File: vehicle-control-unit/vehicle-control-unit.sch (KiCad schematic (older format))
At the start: 22 parts, among them J1 Conn_02x04_Male_UnitPerRow, J2 Conn_01x04_Male, J3 Conn_02x03_Male, J4 Conn_02x03_Male, J5 Conn_02x03_Male, J6 Conn_02x03_Male, U1 Teensy3.2, U2 NRF24L01+ breakout

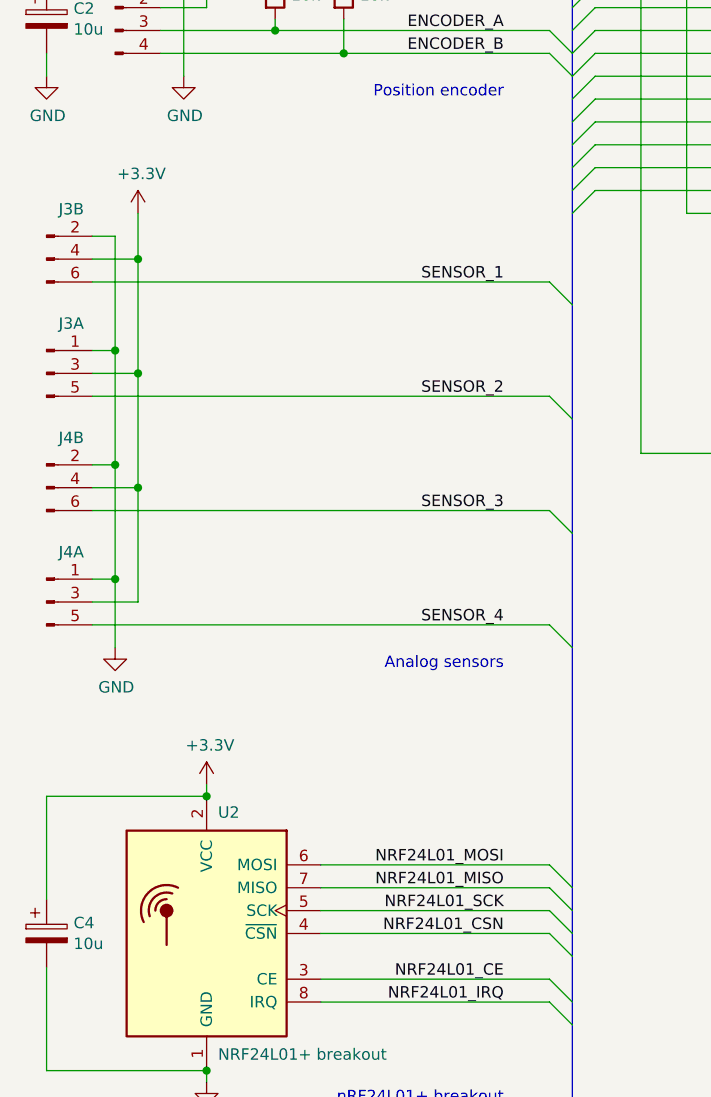
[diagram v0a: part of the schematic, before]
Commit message: Clean up routing
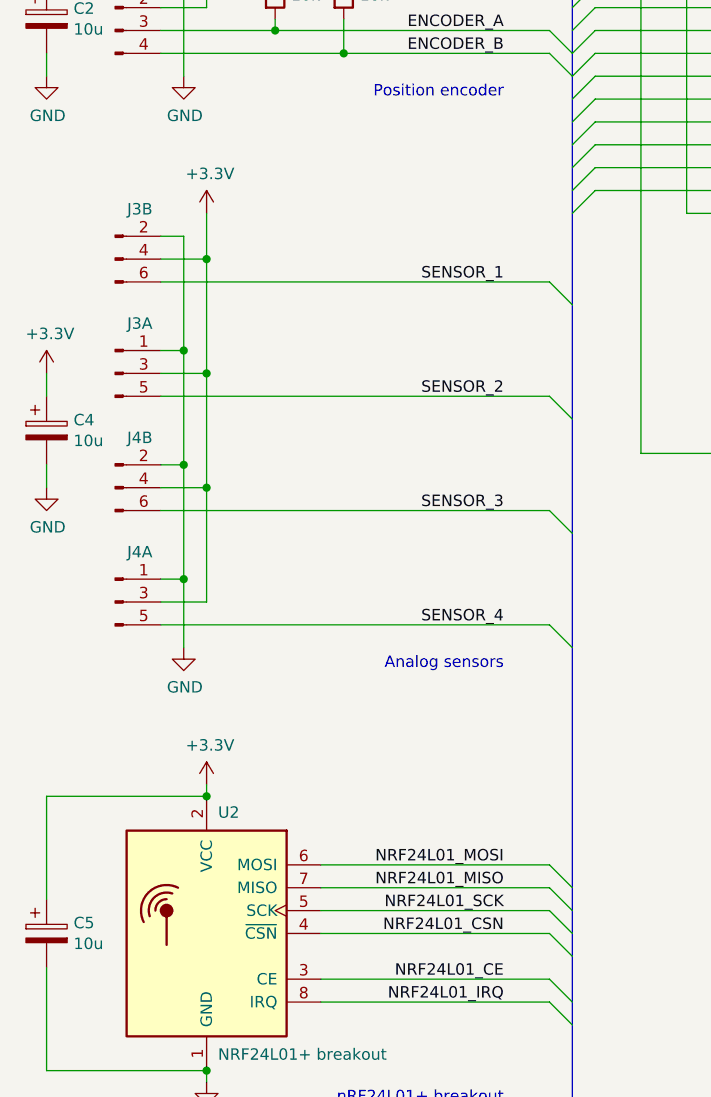
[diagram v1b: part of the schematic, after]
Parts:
- added C4: 10u, Capacitor_THT:CP_Radial_D5.0mm_P2.50mm, symbol Device:CP
- renumbered C4 to C5
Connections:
- net +3V3: now also C4.1
- net GND: now also C4.2
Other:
- moved on the sheet: J3A, J3B, J4A, J4B
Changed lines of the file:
@@
 Sheet 1 3
 Title "Earth Rover"
-Date "2020-06-07"
-Rev "7"
+Date "2020-06-08"
+Rev "8"
 Comp "Vijfendertig BVBA"
 Comment1 "Maarten De Munck"
@@
 	6850 6350 6850 6950
 $Comp
-L power:GND #PWR021
+L power:GND #PWR023
 U 1 1 5DE14910
 P 6850 8250
-F 0 "#PWR021" H 6850 8000 50  0001 C CNN
+F 0 "#PWR023" H 6850 8000 50  0001 C CNN
 F 1 "GND" H 6855 8077 50  0000 C CNN
 F 2 "" H 6850 8250 50  0001 C CNN
@@
 Connection ~ 6650 5950
 $Comp
-L power:+5V #PWR018
+L power:+5V #PWR019
 U 1 1 5DE1FF8F
 P 6650 5850
-F 0 "#PWR018" H 6650 5700 50  0001 C CNN
+F 0 "#PWR019" H 6650 5700 50  0001 C CNN
 F 1 "+5V" H 6665 6023 50  0000 C CNN
 F 2 "" H 6650 5850 50  0001 C CNN
@@
 L earth-rover-symbols:Conn_02x03_Male_UnitPerRow J3
 U 2 1 5DFC88C9
-P 1250 5000
-F 0 "J3" H 1358 5189 50  0000 C BNN
-F 1 "Conn_02x03_Male" H 1358 5190 50  0001 C CNN
-F 2 "Connector_PinHeader_2.54mm:PinHeader_2x03_P2.54mm_Horizontal" H 1250 5000 50  0001 C CNN
-F 3 "~" H 1250 5000 50  0001 C CNN
-	2    1250 5000
-	1    0    0    -1
-$EndComp
-$Comp
-L power:GND #PWR019
+P 1550 5000
+F 0 "J3" H 1658 5189 50  0000 C BNN
+F 1 "Conn_02x03_Male" H 1658 5190 50  0001 C CNN
+F 2 "Connector_PinHeader_2.54mm:PinHeader_2x03_P2.54mm_Horizontal" H 1550 5000 50  0001 C CNN
+F 3 "~" H 1550 5000 50  0001 C CNN
+	2    1550 5000
+	1    0    0    -1
+$EndComp
+$Comp
+L power:GND #PWR021
 U 1 1 5DFCC639
-P 1550 6700
-F 0 "#PWR019" H 1550 6450 50  0001 C CNN
-F 1 "GND" H 1555 6527 50  0000 C CNN
-F 2 "" H 1550 6700 50  0001 C CNN
-F 3 "" H 1550 6700 50  0001 C CNN
-	1    1550 6700
+P 1850 6700
+F 0 "#PWR021" H 1850 6450 50  0001 C CNN
+F 1 "GND" H 1855 6527 50  0000 C CNN
+F 2 "" H 1850 6700 50  0001 C CNN
+F 3 "" H 1850 6700 50  0001 C CNN
+	1    1850 6700
 	1    0    0    -1
 $EndComp
@@
 L power:+3.3V #PWR016
 U 1 1 5DFCCB63
-P 1650 4800
-F 0 "#PWR016" H 1650 4650 50  0001 C CNN
-F 1 "+3.3V" H 1665 4973 50  0000 C CNN
-F 2 "" H 1650 4800 50  0001 C CNN
-F 3 "" H 1650 4800 50  0001 C CNN
-	1    1650 4800
-	1    0    0    -1
-$EndComp
-Wire Wire Line
-	1450 4900 1550 4900
-Wire Wire Line
-	1550 4900 1550 5400
-Wire Wire Line
-	1450 5000 1650 5000
-Wire Wire Line
-	1650 5000 1650 4800
+P 1950 4800
+F 0 "#PWR016" H 1950 4650 50  0001 C CNN
+F 1 "+3.3V" H 1965 4973 50  0000 C CNN
+F 2 "" H 1950 4800 50  0001 C CNN
+F 3 "" H 1950 4800 50  0001 C CNN
+	1    1950 4800
+	1    0    0    -1
+$EndComp
+Wire Wire Line
+	1750 4900 1850 4900
+Wire Wire Line
+	1850 4900 1850 5400
+Wire Wire Line
+	1750 5000 1950 5000
+Wire Wire Line
+	1950 5000 1950 4800
 $Comp
 L earth-rover-symbols:Conn_02x03_Male_UnitPerRow J3
 U 1 1 5E000766
-P 1250 5500
-F 0 "J3" H 1358 5689 50  0000 C BNN
-F 1 "Conn_02x03_Male" H 1358 5690 50  0001 C CNN
-F 2 "Connector_PinHeader_2.54mm:PinHeader_2x03_P2.54mm_Horizontal" H 1250 5500 50  0001 C CNN
-F 3 "~" H 1250 5500 50  0001 C CNN
-	1    1250 5500
+P 1550 5500
+F 0 "J3" H 1658 5689 50  0000 C BNN
+F 1 "Conn_02x03_Male" H 1658 5690 50  0001 C CNN
+F 2 "Connector_PinHeader_2.54mm:PinHeader_2x03_P2.54mm_Horizontal" H 1550 5500 50  0001 C CNN
+F 3 "~" H 1550 5500 50  0001 C CNN
+	1    1550 5500
 	1    0    0    -1
 $EndComp
@@
 L earth-rover-symbols:Conn_02x03_Male_UnitPerRow J4
 U 2 1 5E000E2E
-P 1250 6000
-F 0 "J4" H 1358 6189 50  0000 C BNN
-F 1 "Conn_02x03_Male" H 1358 6190 50  0001 C CNN
-F 2 "Connector_PinHeader_2.54mm:PinHeader_2x03_P2.54mm_Horizontal" H 1250 6000 50  0001 C CNN
-F 3 "~" H 1250 6000 50  0001 C CNN
-	2    1250 6000
+P 1550 6000
+F 0 "J4" H 1658 6189 50  0000 C BNN
+F 1 "Conn_02x03_Male" H 1658 6190 50  0001 C CNN
+F 2 "Connector_PinHeader_2.54mm:PinHeader_2x03_P2.54mm_Horizontal" H 1550 6000 50  0001 C CNN
+F 3 "~" H 1550 6000 50  0001 C CNN
+	2    1550 6000
 	1    0    0    -1
 $EndComp
@@
 L earth-rover-symbols:Conn_02x03_Male_UnitPerRow J4
 U 1 1 5E0013EA
-P 1250 6500
-F 0 "J4" H 1358 6689 50  0000 C BNN
-F 1 "Conn_02x03_Male" H 1358 6690 50  0001 C CNN
-F 2 "Connector_PinHeader_2.54mm:PinHeader_2x03_P2.54mm_Horizontal" H 1250 6500 50  0001 C CNN
-F 3 "~" H 1250 6500 50  0001 C CNN
-	1    1250 6500
-	1    0    0    -1
-$EndComp
-Wire Wire Line
-	1450 5400 1550 5400
-Connection ~ 1550 5400
-Wire Wire Line
-	1550 5400 1550 5900
-Wire Wire Line
-	1450 5900 1550 5900
-Connection ~ 1550 5900
-Wire Wire Line
-	1550 5900 1550 6400
-Wire Wire Line
-	1450 6400 1550 6400
-Connection ~ 1550 6400
-Wire Wire Line
-	1550 6400 1550 6700
-Wire Wire Line
-	1650 5000 1650 5500
-Wire Wire Line
-	1650 5500 1450 5500
-Connection ~ 1650 5000
-Wire Wire Line
-	1650 5500 1650 6000
-Wire Wire Line
-	1650 6000 1450 6000
-Connection ~ 1650 5500
-Wire Wire Line
-	1650 6000 1650 6500
-Wire Wire Line
-	1650 6500 1450 6500
-Connection ~ 1650 6000
-$Comp
-L power:GND #PWR022
+P 1550 6500
+F 0 "J4" H 1658 6689 50  0000 C BNN
+F 1 "Conn_02x03_Male" H 1658 6690 50  0001 C CNN
+F 2 "Connector_PinHeader_2.54mm:PinHeader_2x03_P2.54mm_Horizontal" H 1550 6500 50  0001 C CNN
+F 3 "~" H 1550 6500 50  0001 C CNN
+	1    1550 6500
+	1    0    0    -1
+$EndComp
+Wire Wire Line
+	1750 5400 1850 5400
+Connection ~ 1850 5400
+Wire Wire Line
+	1850 5400 1850 5900
+Wire Wire Line
+	1750 5900 1850 5900
+Connection ~ 1850 5900
+Wire Wire Line
+	1850 5900 1850 6400
+Wire Wire Line
+	1750 6400 1850 6400
+Connection ~ 1850 6400
+Wire Wire Line
+	1850 6400 1850 6700
+Wire Wire Line
+	1950 5000 1950 5500
+Wire Wire Line
+	1950 5500 1750 5500
+Connection ~ 1950 5000
+Wire Wire Line
+	1950 5500 1950 6000
+Wire Wire Line
+	1950 6000 1750 6000
+Connection ~ 1950 5500
+Wire Wire Line
+	1950 6000 1950 6500
+Wire Wire Line
+	1950 6500 1750 6500
+Connection ~ 1950 6000
+$Comp
+L power:GND #PWR024
 U 1 1 5DFBDB8E
 P 1950 8600
-F 0 "#PWR022" H 1950 8350 50  0001 C CNN
+F 0 "#PWR024" H 1950 8350 50  0001 C CNN
 F 1 "GND" H 1955 8427 50  0000 C CNN
 F 2 "" H 1950 8600 50  0001 C CNN
@@
 $EndComp
 $Comp
-L power:+3.3V #PWR020
+L power:+3.3V #PWR022
 U 1 1 5DFBD20A
 P 1950 7300
-F 0 "#PWR020" H 1950 7150 50  0001 C CNN
+F 0 "#PWR022" H 1950 7150 50  0001 C CNN
 F 1 "+3.3V" H 1965 7473 50  0000 C CNN
 F 2 "" H 1950 7300 50  0001 C CNN
@@
 $EndComp
 $Comp
-L power:GND #PWR024
+L power:GND #PWR026
 U 1 1 5E17642F
 P 1350 9700
-F 0 "#PWR024" H 1350 9450 50  0001 C CNN
+F 0 "#PWR026" H 1350 9450 50  0001 C CNN
 F 1 "GND" H 1355 9527 50  0000 C CNN
 F 2 "" H 1350 9700 50  0001 C CNN
@@
 $EndComp
 $Comp
-L power:+3.3V #PWR023
+L power:+3.3V #PWR025
 U 1 1 5E177C83
 P 1950 9200
-F 0 "#PWR023" H 1950 9050 50  0001 C CNN
+F 0 "#PWR025" H 1950 9050 50  0001 C CNN
 F 1 "+3.3V" H 1965 9373 50  0000 C CNN
 F 2 "" H 1950 9200 50  0001 C CNN
@@
 $EndComp
 $Comp
-L Device:CP C4
+L Device:CP C5
 U 1 1 5DE41454
 P 1250 7950
-F 0 "C4" H 1368 7996 50  0000 L CNN
+F 0 "C5" H 1368 7996 50  0000 L CNN
 F 1 "10u" H 1368 7905 50  0000 L CNN
 F 2 "Capacitor_THT:CP_Radial_D5.0mm_P2.50mm" H 1288 7800 50  0001 C CNN
@@
 	1950 9600 3450 9600
 Wire Wire Line
-	1450 6600 3450 6600
-Wire Wire Line
-	1450 6100 3450 6100
-Wire Wire Line
-	1450 5600 3450 5600
-Wire Wire Line
-	1450 5100 3450 5100
+	1750 6600 3450 6600
+Wire Wire Line
+	1750 6100 3450 6100
+Wire Wire Line
+	1750 5600 3450 5600
+Wire Wire Line
+	1750 5100 3450 5100
 Wire Wire Line
 	2550 2800 3450 2800
@@
 Text Notes 3250 4300 2    50   ~ 0
 Position encoder
+$Comp
+L Device:CP C4
+U 1 1 5EE06376
+P 1250 5750
+F 0 "C4" H 1368 5796 50  0000 L CNN
+F 1 "10u" H 1368 5705 50  0000 L CNN
+F 2 "Capacitor_THT:CP_Radial_D5.0mm_P2.50mm" H 1288 5600 50  0001 C CNN
+F 3 "~" H 1250 5750 50  0001 C CNN
+	1    1250 5750
+	1    0    0    -1
+$EndComp
+$Comp
+L power:GND #PWR020
+U 1 1 5EE0637C
+P 1250 6000
+F 0 "#PWR020" H 1250 5750 50  0001 C CNN
+F 1 "GND" H 1255 5827 50  0000 C CNN
+F 2 "" H 1250 6000 50  0001 C CNN
+F 3 "" H 1250 6000 50  0001 C CNN
+	1    1250 6000
+	1    0    0    -1
+$EndComp
+$Comp
+L power:+3.3V #PWR018
+U 1 1 5EE06382
+P 1250 5500
+F 0 "#PWR018" H 1250 5350 50  0001 C CNN
+F 1 "+3.3V" H 1265 5673 50  0000 C CNN
+F 2 "" H 1250 5500 50  0001 C CNN
+F 3 "" H 1250 5500 50  0001 C CNN
+	1    1250 5500
+	1    0    0    -1
+$EndComp
+Wire Wire Line
+	1250 5900 1250 6000
+Wire Wire Line
+	1250 5500 1250 5600
 Wire Bus Line
 	5150 6250 5150 9900

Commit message: Use larger holes for nRF24L01+ breakout board
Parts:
- U2: footprint RF_Module:nRF24L01_Breakout -> earth-rover-footprints:nRF24L01_Breakout_LargerHoles
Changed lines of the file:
@@
 F 0 "U2" H 1900 8450 50  0000 R BNN
 F 1 "NRF24L01+ breakout" H 1900 7450 50  0000 R TNN
-F 2 "RF_Module:nRF24L01_Breakout" H 2100 8550 50  0001 L CIN
+F 2 "earth-rover-footprints:nRF24L01_Breakout_LargerHoles" H 2100 8550 50  0001 L CIN
 F 3 "http://www.nordicsemi.com/eng/content/download/2730/34105/file/nRF24L01_Product_Specification_v2_0.pdf" H 1950 7850 50  0001 C CNN
 	1    1950 7950
